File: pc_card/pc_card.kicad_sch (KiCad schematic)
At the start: 59 parts, among them IC1 SV 3.3V, IC3 SV 4.5V, IC4 TPA152DR, J1 PCMCIA Connector, J2 Headphones Out, U1 Z8601720ASG, U2 93C56, U3 YMF289B-S, U4 YAC516-E, Y1 4.19MHz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

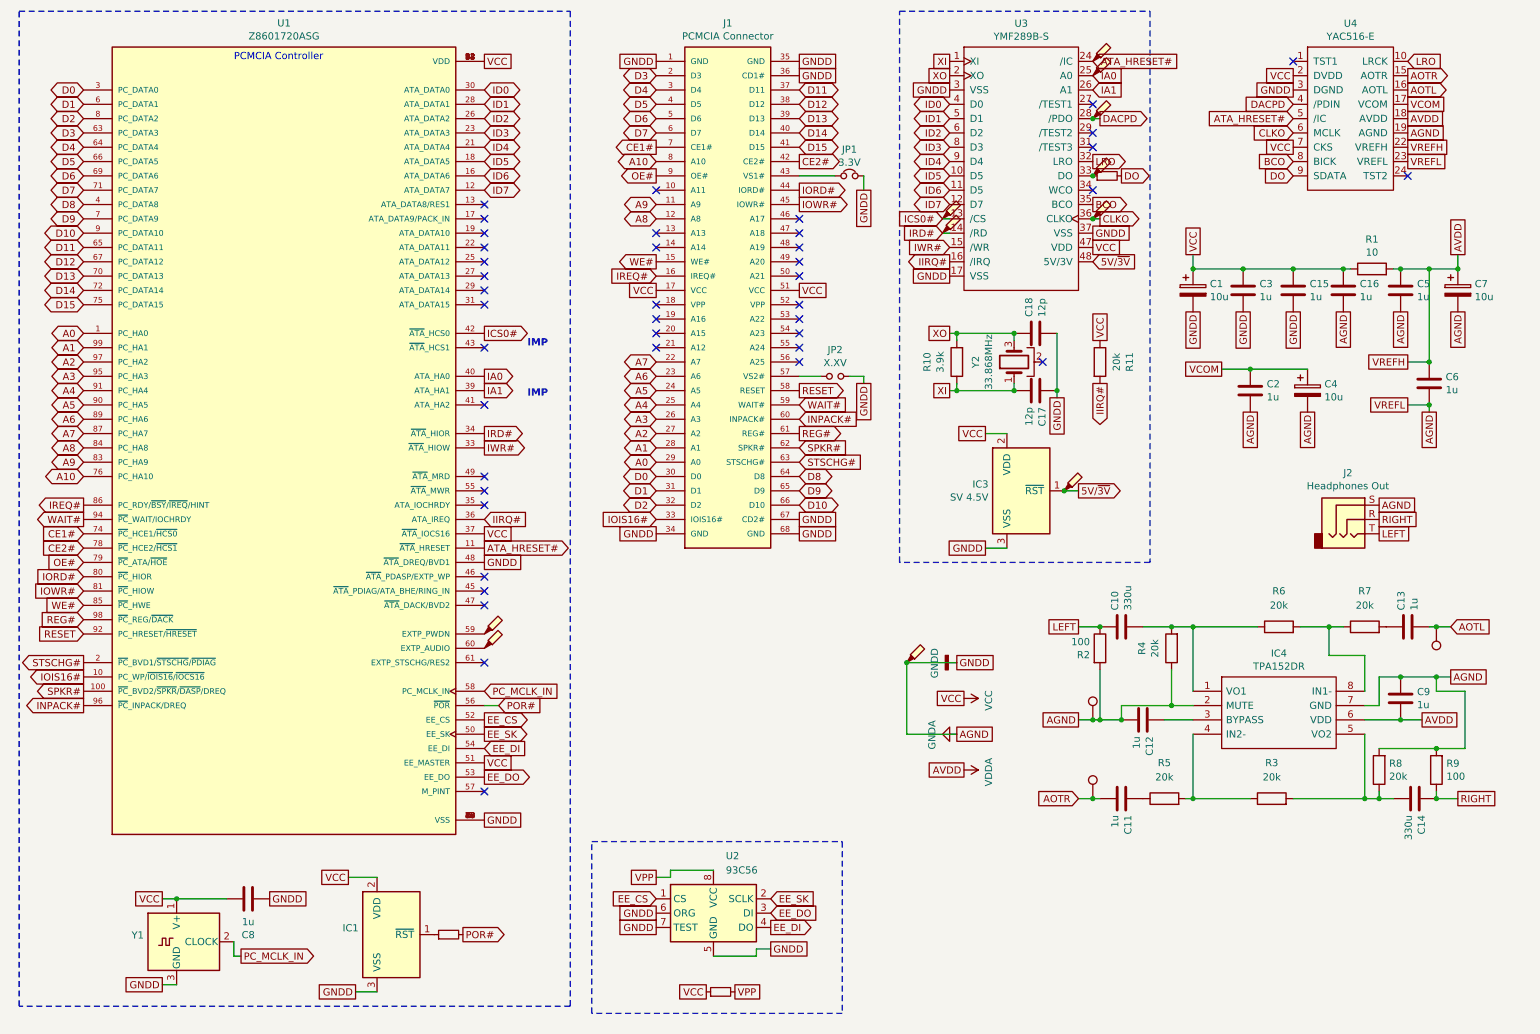
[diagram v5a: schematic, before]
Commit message: socket assembly
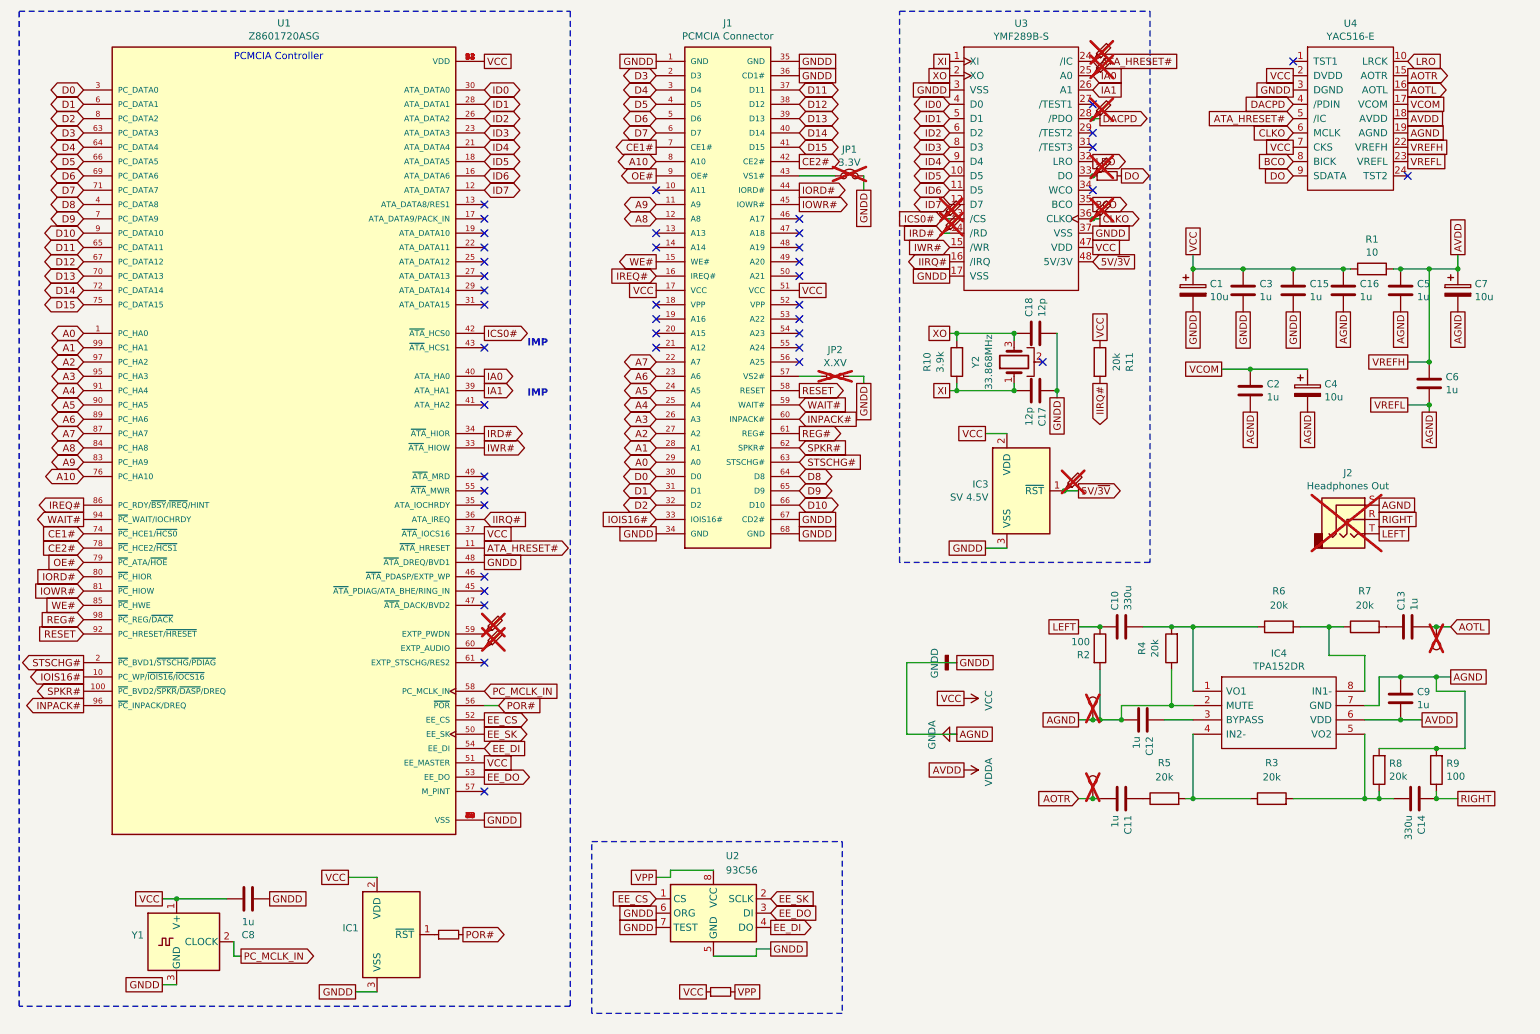
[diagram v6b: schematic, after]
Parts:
- removed TP5: GND, TestPoint:TestPoint_Keystone_5015_Micro-Minature, symbol Connector:TestPoint_Probe
- J2: now not fitted; now left out of the parts list
- JP1, JP2, TP1, TP10, TP11, TP12, TP13, TP14, TP2, TP3, TP4, TP6, TP7, TP8, TP9: now not fitted
- U1: Manufacturer_Part_Number (none) -> Z8601720ASG
- U2: Manufacturer_Part_Number (none) -> 93C56
- U3: Manufacturer_Part_Number (none) -> YMF289B-S
- U4: Manufacturer_Part_Number (none) -> YAC516-E
- Y1: value 4.19MHz -> 8MHZ; Manufacturer_Part_Number MAX7375AXR425+T -> MAX7375AXR805+T
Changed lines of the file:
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@@
 	)
 	(junction
-		(at 173.99 130.81)
-		(diameter 0)
-		(color 0 0 0 0)
-	)
-	(junction
 		(at 267.97 154.94)
 		(diameter 0)
@@
 			)
 		)
-		(property "Manufacturer_Part_Number" "~"
+		(property "Manufacturer_Part_Number" "Z8601720ASG"
 			(at 63.5 90.17 0)
 			(effects
@@
 		(in_bom yes)
 		(on_board yes)
-		(dnp no)
+		(dnp yes)
 		(property "Reference" "JP1"
 			(at 163.83 39.751 0)
@@
 		(in_bom yes)
 		(on_board yes)
-		(dnp no)
+		(dnp yes)
 		(property "Reference" "JP2"
 			(at 161.29 75.311 0)
@@
 			)
 		)
-		(property "Manufacturer_Part_Number" "~"
+		(property "Manufacturer_Part_Number" "YMF289B-S"
 			(at 194.31 21.59 0)
 			(effects
@@
 			)
 		)
-		(property "Manufacturer_Part_Number" "~"
+		(property "Manufacturer_Part_Number" "YAC516-E"
 			(at 252.73 20.32 0)
 			(effects
@@
 		(in_bom yes)
 		(on_board yes)
-		(dnp no)
+		(dnp yes)
 		(property "Reference" "TP1"
 			(at 207.01 150.1648 90)
@@
 		(in_bom yes)
 		(on_board yes)
-		(dnp no)
+		(dnp yes)
 		(property "Reference" "TP2"
 			(at 265.3538 126.2888 90)
@@
 		(unit 1)
 		(exclude_from_sim no)
-		(in_bom yes)
+		(in_bom no)
 		(on_board yes)
-		(dnp no)
+		(dnp yes)
 		(property "Reference" "J2"
 			(at 252.2728 97.155 0)
@@
 			)
 		)
-		(property "Value" "4.19MHz"
+		(property "Value" "8MHZ"
 			(at 38.6334 181.483 0)
 			(effects
@@
 			)
 		)
-		(property "Manufacturer_Part_Number" "MAX7375AXR425+T"
+		(property "Manufacturer_Part_Number" "MAX7375AXR805+T"
 			(at 44.45 180.34 0)
 			(effects
@@
 		(in_bom yes)
 		(on_board yes)
-		(dnp no)
+		(dnp yes)
 		(property "Reference" "TP12"
 			(at 210.82 31.4324 0)
@@
 		(in_bom yes)
 		(on_board yes)
-		(dnp no)
+		(dnp yes)
 		(property "Reference" "TP11"
 			(at 210.82 49.2124 0)
@@
 			)
 		)
+		(property "Manufacturer_Part_Number" "93C56"
+			(at 139.7 175.26 0)
+			(effects
+				(font
+					(size 1.27 1.27)
+				)
+				(hide yes)
+			)
+		)
 		(pin "7"
 		)
@@
 		(in_bom yes)
 		(on_board yes)
-		(dnp no)
+		(dnp yes)
 		(property "Reference" "TP9"
 			(at 210.82 41.5924 0)
@@
 	(symbol
 		(lib_id "Connector:TestPoint_Probe")
-		(at 173.99 130.81 0)
-		(unit 1)
-		(exclude_from_sim no)
-		(in_bom yes)
-		(on_board yes)
-		(dnp no)
-		(property "Reference" "TP5"
-			(at 177.8 127.9524 0)
-			(effects
-				(font
-					(size 1.27 1.27)
-				)
-				(justify left)
-				(hide yes)
-			)
-		)
-		(property "Value" "GND"
-			(at 182.88 130.81 0)
-			(effects
-				(font
-					(size 1.27 1.27)
-				)
-				(justify left)
-				(hide yes)
-			)
-		)
-		(property "Footprint" "TestPoint:TestPoint_Keystone_5015_Micro-Minature"
-			(at 179.07 130.81 0)
-			(effects
-				(font
-					(size 1.27 1.27)
-				)
-				(hide yes)
-			)
-		)
-		(property "Datasheet" "~"
-			(at 179.07 130.81 0)
-			(effects
-				(font
-					(size 1.27 1.27)
-				)
-				(hide yes)
-			)
-		)
-		(property "Description" "test point (alternative probe-style design)"
-			(at 173.99 130.81 0)
-			(effects
-				(font
-					(size 1.27 1.27)
-				)
-				(hide yes)
-			)
-		)
-		(pin "1"
-		)
-		(instances
-			(project "pc_card"
-				(path "/792da158-0192-445f-a668-7902349a051c"
-					(reference "TP5")
-					(unit 1)
-				)
-			)
-		)
-	)
-	(symbol
-		(lib_id "Connector:TestPoint_Probe")
 		(at 99.06 125.73 0)
 		(unit 1)
@@
 		(in_bom yes)
 		(on_board yes)
-		(dnp no)
+		(dnp yes)
 		(property "Reference" "TP6"
 			(at 102.87 122.8724 0)
@@
 		(in_bom yes)
 		(on_board yes)
-		(dnp no)
+		(dnp yes)
 		(property "Reference" "TP3"
 			(at 184.15 49.2124 0)
@@
 		(in_bom yes)
 		(on_board yes)
-		(dnp no)
+		(dnp yes)
 		(property "Reference" "TP4"
 			(at 209.6262 139.1412 90)
@@
 		(in_bom yes)
 		(on_board yes)
-		(dnp no)
+		(dnp yes)
 		(property "Reference" "TP7"
 			(at 102.87 125.4124 0)
@@
 		(in_bom yes)
 		(on_board yes)
-		(dnp no)
+		(dnp yes)
 		(property "Reference" "TP14"
 			(at 210.82 21.2724 0)
@@
 		(in_bom yes)
 		(on_board yes)
-		(dnp no)
+		(dnp yes)
 		(property "Reference" "TP10"
 			(at 184.15 51.7524 0)
@@
 		(in_bom yes)
 		(on_board yes)
-		(dnp no)
+		(dnp yes)
 		(property "Reference" "TP8"
 			(at 205.74 97.4724 0)
@@
 		(in_bom yes)
 		(on_board yes)
-		(dnp no)
+		(dnp yes)
 		(property "Reference" "TP13"
 			(at 210.82 23.8124 0)

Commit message: messing with xtal
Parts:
- Y2: footprint Crystal:Crystal_SMD_2016-4Pin_2.0x1.6mm -> Crystal:Crystal_SMD_2520-4Pin_2.5x2.0mm; symbol Device:Crystal_GND2 -> Device:Crystal_GND24_Small; Manufacturer_Part_Number XRCPB33M868F0L00R0 -> XRCGB33M868F4M00R0; Mouser Part Number 81-XRCPB33M868F0L0R0 -> 81-XRCGB33M868F4M0R0
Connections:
- no-connect marks 42 -> 43
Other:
- moved on the sheet: Y2
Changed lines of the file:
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@@
 	)
 	(no_connect
+		(at 190.5 77.47)
+	)
+	(no_connect
 		(at 99.06 52.07)
 	)
@@
 	)
 	(no_connect
-		(at 198.12 77.47)
+		(at 195.58 77.47)
 	)
 	(no_connect
@@
 	(wire
 		(pts
+			(xy 193.04 80.01) (xy 193.04 82.55)
+		)
+		(stroke
+			(width 0)
+			(type default)
+		)
+	)
+	(wire
+		(pts
 			(xy 267.97 154.94) (xy 267.97 153.67)
 		)
@@
 	(wire
 		(pts
-			(xy 193.04 73.66) (xy 193.04 72.39)
-		)
-		(stroke
-			(width 0)
-			(type default)
-		)
-	)
-	(wire
-		(pts
 			(xy 212.09 138.43) (xy 212.09 140.97)
 		)
@@
 	(wire
 		(pts
-			(xy 193.04 82.55) (xy 193.04 81.28)
-		)
-		(stroke
-			(width 0)
-			(type default)
-		)
-	)
-	(wire
-		(pts
 			(xy 173.99 130.81) (xy 173.99 143.51)
 		)
@@
 	(wire
 		(pts
+			(xy 193.04 72.39) (xy 193.04 74.93)
+		)
+		(stroke
+			(width 0)
+			(type default)
+		)
+	)
+	(wire
+		(pts
 			(xy 248.92 129.54) (xy 248.92 124.46)
 		)
@@
 	)
 	(symbol
-		(lib_id "Device:Crystal_GND2")
+		(lib_id "Device:Crystal_GND24_Small")
 		(at 193.04 77.47 90)
 		(unit 1)
@@
 			)
 		)
-		(property "Footprint" "Crystal:Crystal_SMD_2016-4Pin_2.0x1.6mm"
+		(property "Footprint" "Crystal:Crystal_SMD_2520-4Pin_2.5x2.0mm"
 			(at 193.04 77.47 0)
 			(effects
@@
 			)
 		)
-		(property "Datasheet" "https://www.mouser.co.uk/datasheet/2/281/1/SPEC_XRCPB33M868F0L00R0-2580714.pdf"
+		(property "Datasheet" "~"
 			(at 193.04 77.47 0)
 			(effects
@@
 			)
 		)
-		(property "Description" ""
+		(property "Description" "Four pin crystal, GND on pins 2 and 4, small symbol"
 			(at 193.04 77.47 0)
 			(effects
@@
 			)
 		)
-		(property "Manufacturer_Part_Number" "XRCPB33M868F0L00R0"
+		(property "Manufacturer_Part_Number" "XRCGB33M868F4M00R0"
 			(at 193.04 77.47 0)
 			(effects
@@
 			)
 		)
-		(property "Mouser Part Number" "81-XRCPB33M868F0L0R0"
+		(property "Mouser Part Number" "81-XRCGB33M868F4M0R0"
 			(at 193.04 77.47 0)
 			(effects
@@
 		(pin "3"
 		)
+		(pin "4"
+		)
 		(instances

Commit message: INF file
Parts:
- removed C5: 1u, Capacitor_SMD:C_1206_3216Metric_Pad1.33x1.80mm_HandSolder, symbol Device:C
- added H1, H2: MountingHole, symbol Mechanical:MountingHole
- added R13: 100k, Resistor_SMD:R_0805_2012Metric_Pad1.20x1.40mm_HandSolder, symbol Device:R
- added TP5: AMP, TestPoint:TestPoint_Pad_1.0x1.0mm, symbol Connector:TestPoint_Probe
- C1, C4, C7: Mouser Price/Stock https://www.mouser.co.uk/ProductDetail/667-EEF-CS1D100R -> (none)
- C10, C14: Mouser Price/Stock https://www.mouser.co.uk/ProductDetail/81-GRM32EC80E337ME5L -> (none)
- C11, C12, C13, C9: Mouser Price/Stock https://www.mouser.co.uk/ProductDetail/80-C0805C105M3RECLR -> (none)
- C15, C16, C2, C3, C6, C8: Mouser Price/Stock https://www.mouser.co.uk/ProductDetail/80-C1206X104G4HACTU -> (none)
- C17, C18: footprint Capacitor_SMD:C_0201_0603Metric_Pad0.64x0.40mm_HandSolder -> Capacitor_SMD:C_0603_1608Metric_Pad1.08x0.95mm_HandSolder; Manufacturer_Name Murata -> KYOCERA-AVX; Manufacturer_Part_Number GJM0335G2A120GB01D -> 0603ZA120JAT2A; Mouser Part Number GJM0335G2A120GB01D -> 581-0603ZA120JAT2A; Mouser Price/Stock https://www.mouser.co.uk/ProductDetail/81-GJM0335G2A120GB1D -> (none)
- IC1: Mouser Price/Stock https://www.mouser.co.uk/ProductDetail/Texas-Instruments/TL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 -> (none)
- IC4: Mouser Price/Stock https://www.mouser.co.uk/ProductDetail/595-TPA152DR -> (none)
- J1: Mouser Price/Stock https://www.mouser.co.uk/ProductDetail/798-IC1F68RD127SF52 -> (none)
- J2: value Headphones Out -> Sound Out; footprint Connector_PinHeader_1.27mm:PinHeader_1x03_P1.27mm_Vertical -> SJ1-2533-SMT-TR:CUI_SJ1-2533-SMT-TR; now fitted; now in the parts list
- R10: Mouser Price/Stock https://www.mouser.co.uk/ProductDetail/667-ERJ-XGNJ392Y -> (none)
- Y1: Mouser Price/Stock https://www.mouser.co.uk/ProductDetail/700-MAX7375AXR425T -> (none)
- Y2: Mouser Price/Stock https://www.mouser.co.uk/ProductDetail/81-XRCPB33M868F0L0R0 -> (none)
- renumbered IC3 to IC2
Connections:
- net AOTL: no longer TP2.1
- net AOTR: now also C11.1; no longer C11.2, TP1.1
- net GNDA: now also R13.1; no longer IC4.2 (MUTE)
- net at C14.2, IC4.5 (VO2), R8.1: now also R3.1; no longer R3.2
- net at R5.1: now also IC4.4 (IN2-), R3.2; no longer C11.1
- net at C13.1, R7.2: now also TP2.1
- net LEFT renamed AMP.LEFT
- net RIGHT renamed AMP.RIGHT
- new net: C11.2, R5.2, TP1.1
- new net MUTE: IC4.2 (MUTE), R13.2, TP5.1
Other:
- moved on the sheet: C10, C11, C12, C13, C14, C9, IC4, R2, R3, R4, R5, R6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
